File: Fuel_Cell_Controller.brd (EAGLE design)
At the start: 203.2 x 163.8 mm, 127 parts, among them J1 BLUETOOTH, U1 MAX232PTH

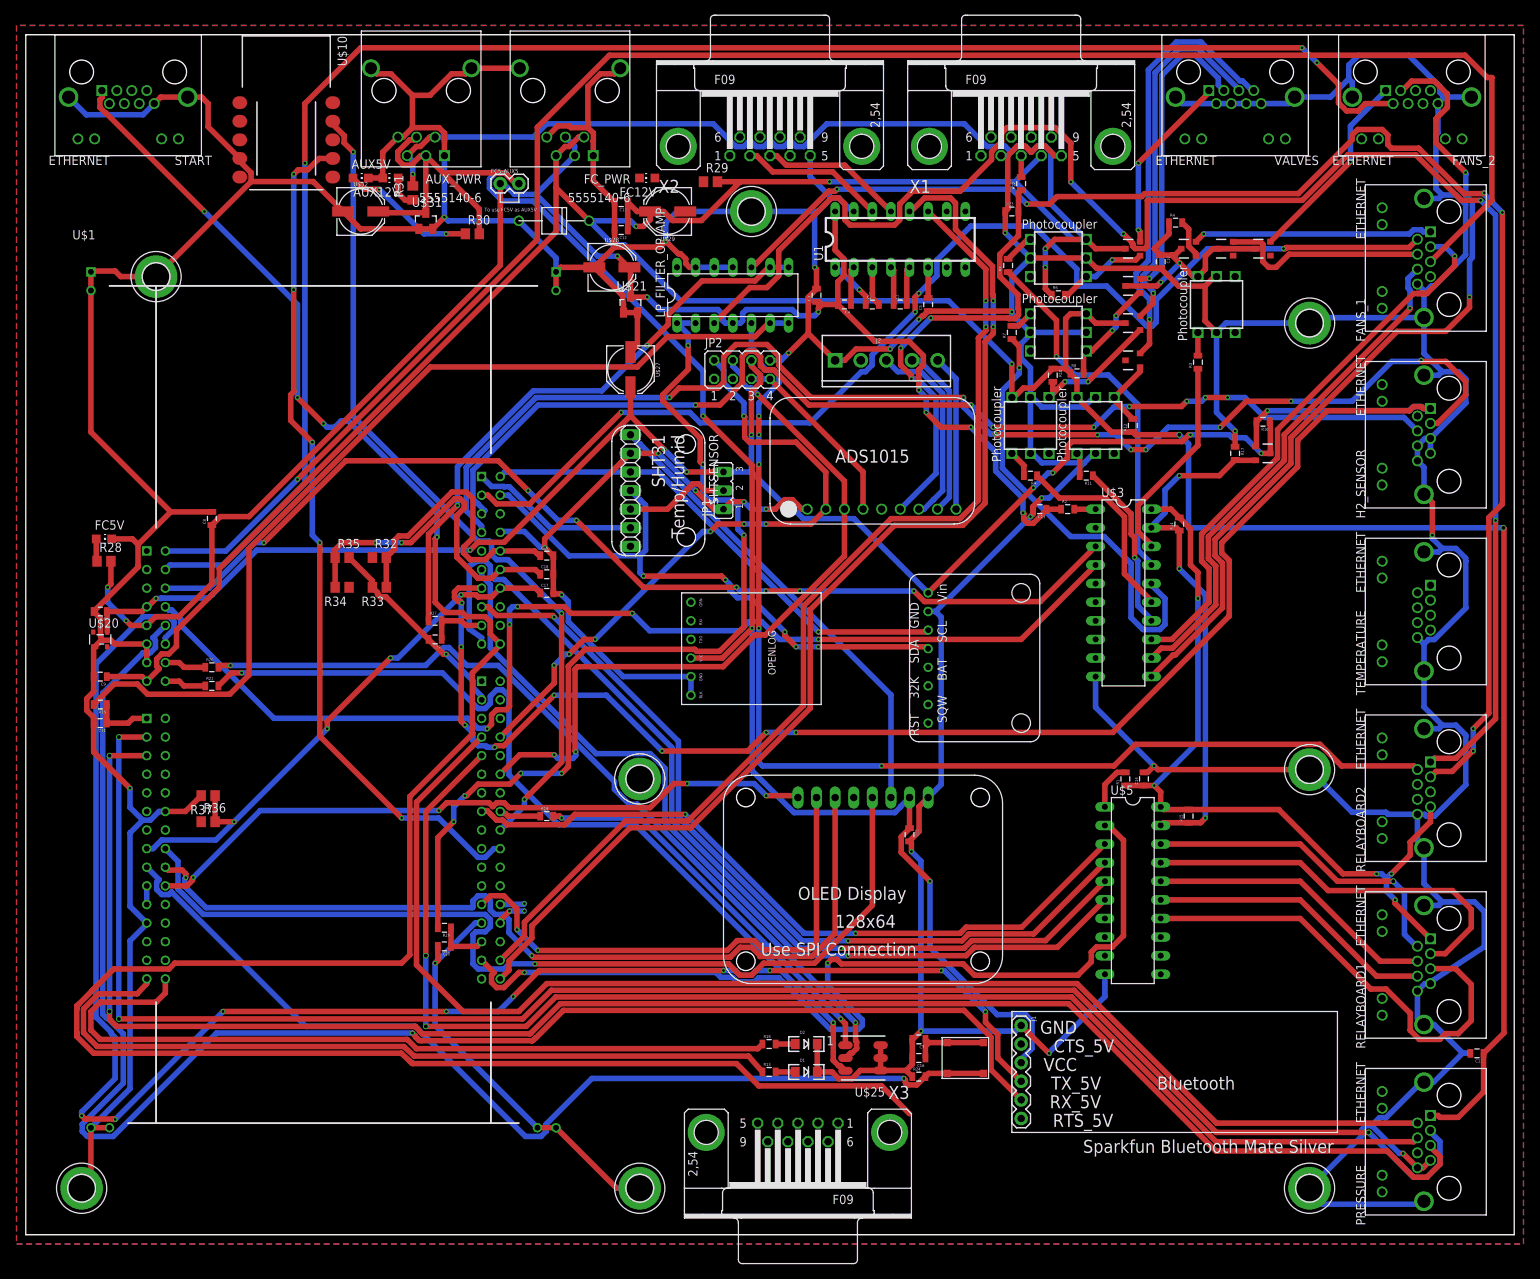
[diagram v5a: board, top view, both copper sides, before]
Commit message: Routing complete! Need to check the two airwires between nucleo pins
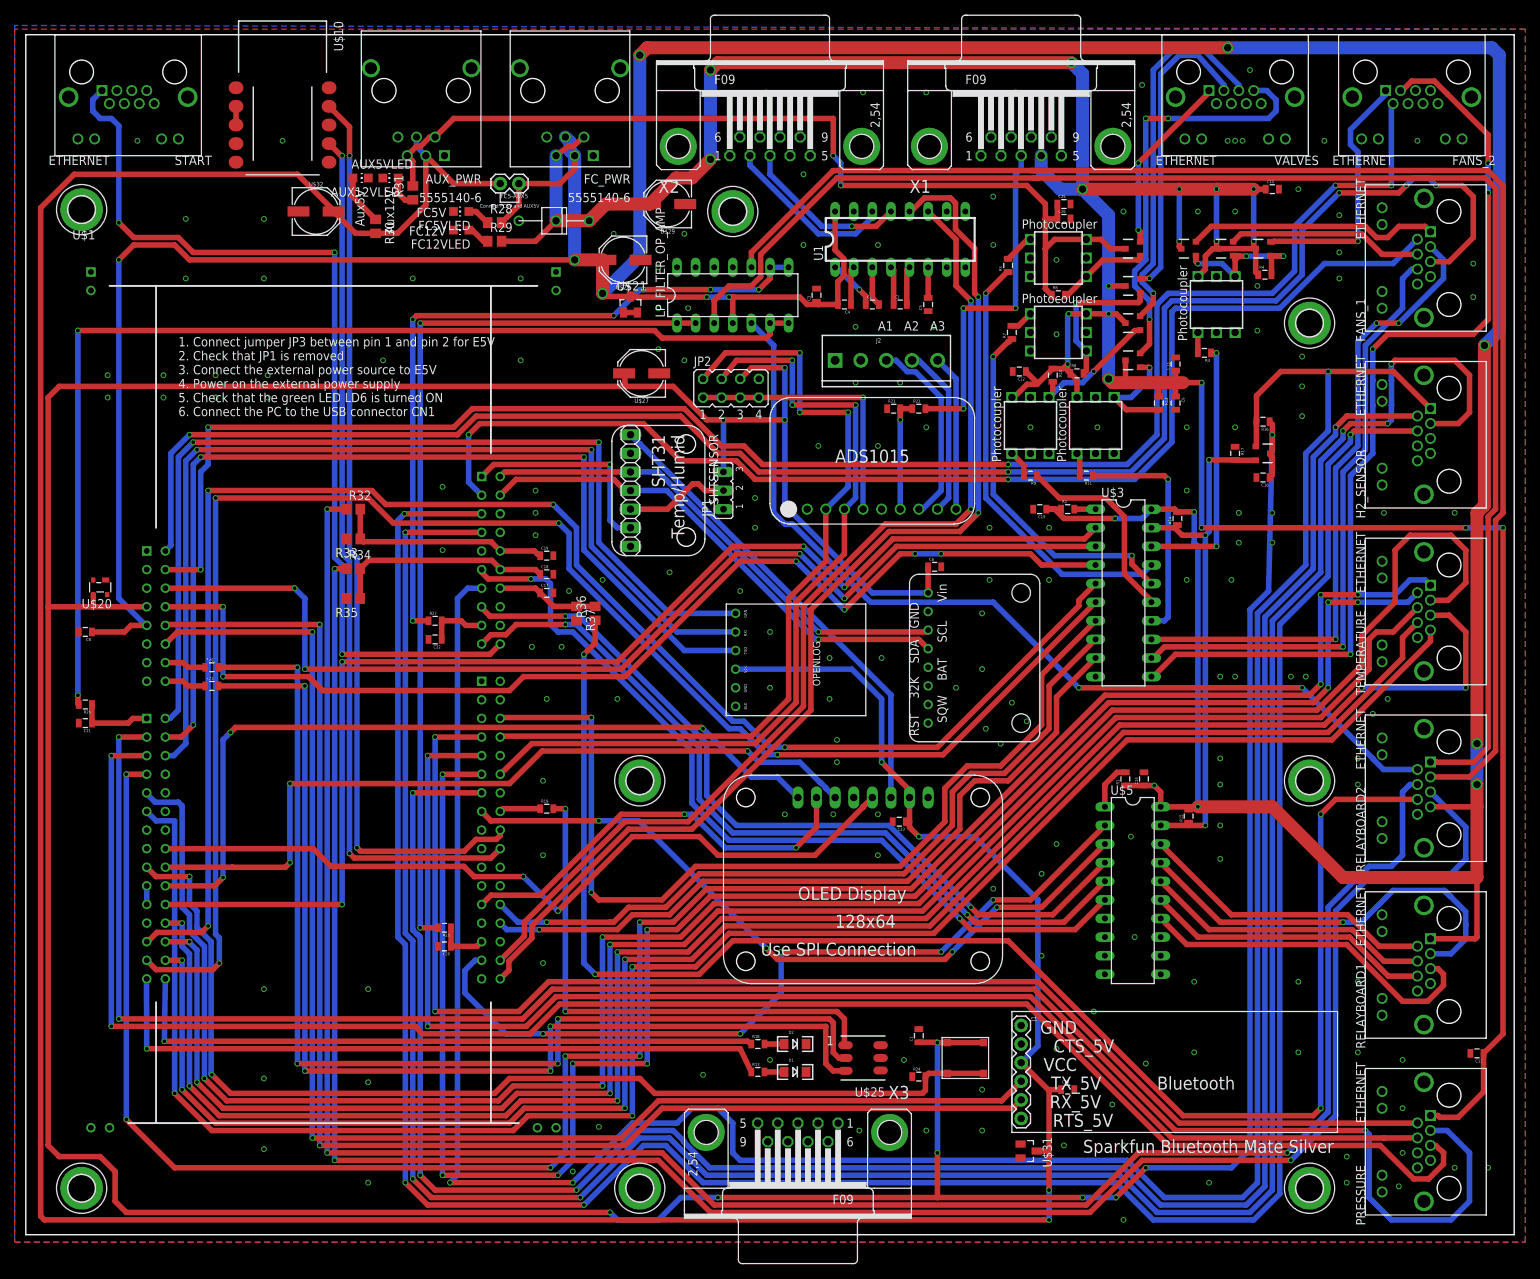
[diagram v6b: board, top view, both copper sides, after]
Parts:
- removed FC12V, FC5V: (no value), led:CHIP-LED0805
- added C24: 1µF, SparkFun-Capacitors:0805
- added C25, C26: 10µF, SparkFun-Capacitors:0805
- added FC12VLED, FC5VLED: (no value), led:CHIP-LED0805
- moved C9 151.5 mm to (157.0, 113.5), turned to 270 degrees
- moved U$31 151.3 mm to (136.9, 11.4), turned to 270 degrees
- moved C6 114.1 mm to (124.1, 91.2), turned to 0 degrees
- moved C16 92.1 mm to (168.9, 103.4)
- moved C13 78.9 mm to (157.0, 118.9), turned to 90 degrees
- moved R28 70.6 mm to (64.0, 138.2)
- moved R36 60.0 mm to (77.7, 84.8), turned to 90 degrees
- moved C12 57.7 mm to (135.6, 117.9)
- moved R37 56.1 mm to (75.2, 84.8), turned to 270 degrees
- moved R22 33.8 mm to (121.9, 112.8), turned to 0 degrees
- moved R23 31.4 mm to (118.5, 112.8)
- moved R29 30.6 mm to (64.0, 135.6)
- moved C8 23.2 mm to (8.13, 82.3), turned to 180 degrees
- moved C10 18.2 mm to (170.2, 142.7), turned to 0 degrees
- moved R4 14.1 mm to (169.2, 131.1)
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- renumbered AUX12V to AUX12VLED, AUX5V to AUX5VLED
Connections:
- net AUX12V: now also C25.1, C26.1
- net AUX5V: now also C24.1
- net FC12V: no longer U$1.VIN
- net GND: now also C24.2, C25.2, C26.2, FC12VLED.C, FC5VLED.C; no longer FC12V.C, FC5V.C
- net N$21: now also FC5VLED.A; no longer FC5V.A
- net N$23: now also FC12VLED.A; no longer FC12V.A
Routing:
- net GND: track 1358.4 -> 1.90 mm, vias 26 -> 171
- net NUC_3V3: track 228.6 -> 594.4 mm, vias 9 -> 11
- net H2_OK: track 0.00 -> 306.3 mm, vias 0 -> 4
- net FCTEMP_1: track 0.00 -> 289.8 mm, vias 0 -> 9
- net _FC_CURR: track 0.00 -> 287.5 mm, vias 0 -> 3
- net _MOTOR_CURR: track 0.00 -> 287.2 mm, vias 0 -> 3
- net FC5V: track 342.4 -> 622.2 mm
- net TEMP_1: track 0.00 -> 279.1 mm, vias 0 -> 3
- net TEMP_5: track 0.00 -> 256.2 mm, vias 0 -> 3
- net FCTEMP_2: track 0.00 -> 251.4 mm, vias 0 -> 9
- net TEMP_3: track 0.00 -> 250.4 mm, vias 0 -> 6
- net AUX5V: track 232.9 -> 469.0 mm, vias 3 -> 4
- net TEMP_2: track 0.00 -> 233.6 mm, vias 0 -> 4
- net TEMP_4: track 0.00 -> 232.3 mm, vias 0 -> 4
- net _OUTPUT_2: track 0.00 -> 220.6 mm, vias 0 -> 4
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- added copper zone on layer 16, net GND
- removed copper zone on layer 16, net N$15
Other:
- board text added: "1. Connect jumper JP3 between pin 1 and pin 2 for E5V 2. Check that JP1 is removed 3. Connect the external power source to E5V 4. Power on the external power supply 5. Check that the green LED LD6 is turned ON 6. Connect the PC to the USB connector CN1"
- board text added: "A1"
- board text added: "A2"
- board text added: "A3"
- board text added: "Aux12V"
- board text added: "Aux5V"
- board text added: "Connect FC5V and AUX5V"
- board text added: "FC12V"
- board text added: "FC5V"
- board text removed: "To use FC5V as AUX5V"

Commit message: Some Updates
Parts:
- added D3, D4, D5, D6, D7, D8, D9: (no value), diode:DO214AC
- added R38: 1kΩ, SparkFun-Passives:0805
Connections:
- net FAN1_PWR: now also D7.C
- net FAN2_PWR: now also D8.C
- net FAN3_PWR: now also D9.C
- net GND: now also D3.A, D4.A, D5.A, D6.A, D7.A, D8.A, D9.A
- net NUC_3V3: now also R38.2
- net OUTPUT_1_ENET: now also D5.C
- net OUTPUT_2_ENET: now also D3.C
- net PURGE_VALVE_ENET: now also D6.C
- net SUPPLY_VALVE_ENET: now also D4.C
- net _START: now also R38.1
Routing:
- net FAN1_PWR: track 34.5 -> 42.9 mm
- net FAN2_PWR: track 26.8 -> 34.6 mm
- net NUC_3V3: track 594.4 -> 598.5 mm, vias 11 -> 12
- net OUTPUT_1_ENET: track 51.4 -> 55.2 mm
- net PURGE_VALVE_ENET: track 42.2 -> 45.2 mm, vias 1 -> 3
- net OUTPUT_2_ENET: track 57.4 -> 59.8 mm
- net _START: track 129.5 -> 131.2 mm
- net FAN3_PWR: track 35.0 -> 36.5 mm
- net SUPPLY_VALVE_ENET: track 24.7 -> 25.7 mm
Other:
- board text added: "1. Connect jumper JP3 between pin 1 and pin 2 for E5V 2. Check that JP1 is removed 3. Connect the external power source to E5V"
- board text added: "4. Power on the external power supply 5. Check that the green LED LD6 is turned ON 6. Connect the PC to the USB connector CN1"
- board text removed: "1. Connect jumper JP3 between pin 1 and pin 2 for E5V 2. Check that JP1 is removed 3. Connect the external power source to E5V 4. Power on the external power supply 5. Check that the green LED LD6 is turned ON 6. Connect the PC to the USB connector CN1"

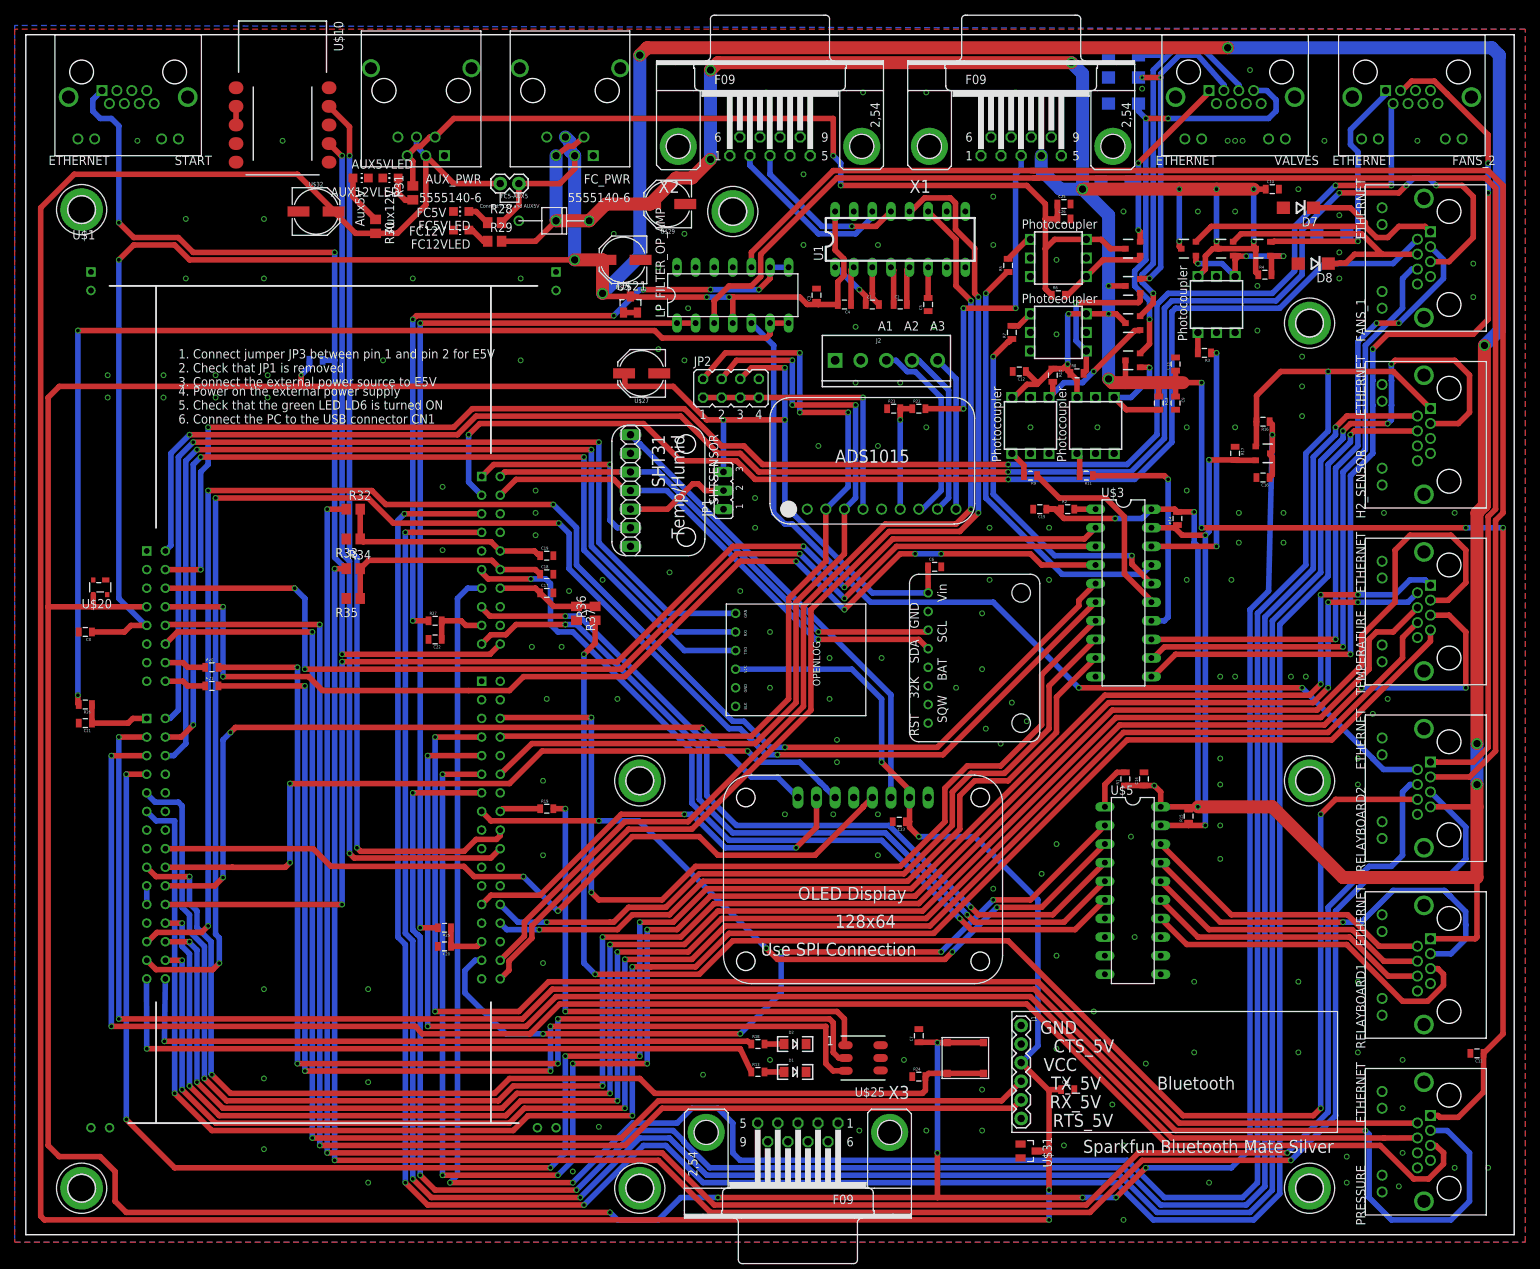
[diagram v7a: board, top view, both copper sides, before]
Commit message: Started Cleaning up the Silk Screen
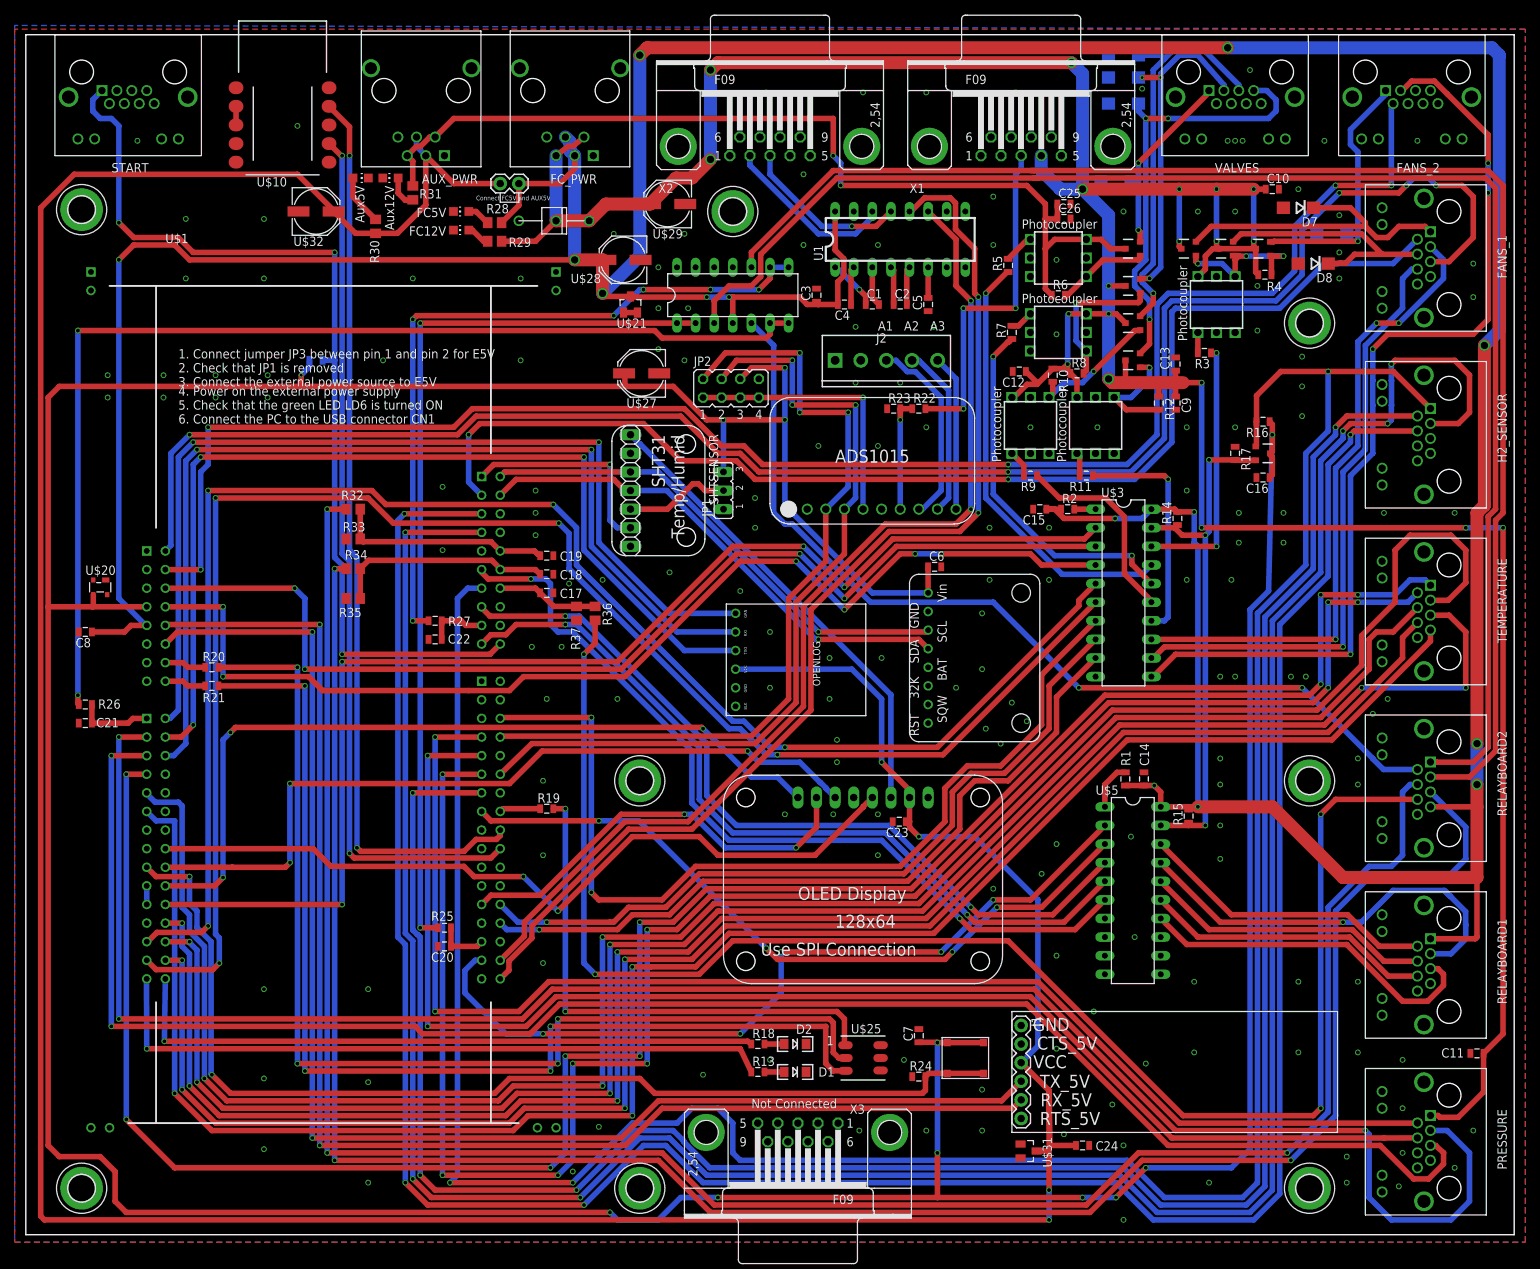
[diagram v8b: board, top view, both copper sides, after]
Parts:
- moved C24 7.89 mm to (144.3, 12.2)
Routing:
- net AUX5V: track 469.0 -> 478.4 mm
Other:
- board text added: "Not Connected"
